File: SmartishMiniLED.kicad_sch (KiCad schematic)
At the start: 35 parts, among them J1 USB_C_Receptacle_USB2.0, J2 BUTTON, J3 Screw_Terminal_01x03, J4 Conn_01x02, P1 NeopixelStripPads, P2 NeopixelStripPads, Q1 MMBT2222, Q2 MMBT2222, Q3 IRLML6344, Q4 IRF7410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

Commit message: Added LCSC part numbers
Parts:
- C6: LCSC (none) -> C176684
- F1: LCSC (none) -> C207041
- Q1, Q2: LCSC (none) -> C2891810
- Q4: LCSC C152423 -> C148144
- R1: LCSC C17407 -> C149504
- R2, R3, R8, R9: LCSC C17617 -> C17414
- R5, R6: LCSC C139928 -> C27834
- R7: LCSC C17617 -> C352224
- U1: LCSC (none) -> C473012
- U4: LCSC C17724 -> C23654
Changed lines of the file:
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@@
       (effects (font (size 1.27 1.27)) hide)
     )
-    (property "LCSC" "C17407" (id 4) (at 67.31 40.64 0)
+    (property "LCSC" "C149504" (id 4) (at 67.31 40.64 0)
       (effects (font (size 1.27 1.27)) hide)
     )
@@
       (effects (font (size 1.27 1.27)) hide)
     )
-    (property "LCSC" "C17617" (id 4) (at 106.68 154.94 0)
+    (property "LCSC" "C17414" (id 4) (at 106.68 154.94 0)
       (effects (font (size 1.27 1.27)) hide)
     )
@@
       (effects (font (size 1.27 1.27)) hide)
     )
-    (property "LCSC" "C17617" (id 4) (at 106.68 176.53 0)
+    (property "LCSC" "C17414" (id 4) (at 106.68 176.53 0)
       (effects (font (size 1.27 1.27)) hide)
     )
@@
       (effects (font (size 1.27 1.27)) hide)
     )
-    (property "LCSC" "C139928" (id 4) (at 210.82 129.54 0)
+    (property "LCSC" "C27834" (id 4) (at 210.82 129.54 0)
       (effects (font (size 1.27 1.27)) hide)
     )
@@
       (effects (font (size 1.27 1.27)) hide)
     )
-    (property "LCSC" "C139928" (id 4) (at 219.71 129.54 0)
+    (property "LCSC" "C27834" (id 4) (at 219.71 129.54 0)
       (effects (font (size 1.27 1.27)) hide)
     )
@@
       (effects (font (size 1.27 1.27)) (justify left) hide)
     )
+    (property "LCSC" "C2891810" (id 4) (at 125.73 154.94 0)
+      (effects (font (size 1.27 1.27)) hide)
+    )
     (pin "1")
     (pin "2")
@@
     (property "Datasheet" "https://www.onsemi.com/pub/Collateral/2N3903-D.PDF" (id 3) (at 125.73 176.53 0)
       (effects (font (size 1.27 1.27)) (justify left) hide)
+    )
+    (property "LCSC" "C2891810" (id 4) (at 125.73 176.53 0)
+      (effects (font (size 1.27 1.27)) hide)
     )
     (pin "1")
@@
       (effects (font (size 1.27 1.27)) hide)
     )
-    (property "LCSC" "C17617" (id 4) (at 104.775 119.38 90)
+    (property "LCSC" "C352224" (id 4) (at 104.775 119.38 90)
       (effects (font (size 1.6002 1.6002)) hide)
     )
@@
     )
     (property "Datasheet" "https://www.espressif.com/sites/default/files/documentation/esp32-wroom-32d_esp32-wroom-32u_datasheet_en.pdf" (id 3) (at 43.18 107.95 0)
+      (effects (font (size 1.27 1.27)) hide)
+    )
+    (property "LCSC" "C473012" (id 4) (at 50.8 109.22 0)
       (effects (font (size 1.27 1.27)) hide)
     )
@@
       (effects (font (size 1.27 1.27)) hide)
     )
+    (property "LCSC" "C207041" (id 4) (at 207.01 115.57 0)
+      (effects (font (size 1.27 1.27)) hide)
+    )
     (pin "1")
     (pin "2")
@@
       (effects (font (size 1.27 1.27)) hide)
     )
-    (property "LCSC" "C17617" (id 4) (at 124.46 102.87 0)
+    (property "LCSC" "C17414" (id 4) (at 124.46 102.87 0)
       (effects (font (size 1.6002 1.6002)) hide)
     )
@@
       (effects (font (size 1.27 1.27)) hide)
     )
-    (property "LCSC" "C17617" (id 4) (at 112.395 125.73 0)
+    (property "LCSC" "C17414" (id 4) (at 112.395 125.73 0)
       (effects (font (size 1.6002 1.6002)) hide)
     )
@@
     )
     (property "Datasheet" "~" (id 3) (at 264.16 80.01 0)
+      (effects (font (size 1.27 1.27)) hide)
+    )
+    (property "LCSC" "C176684" (id 4) (at 264.16 80.01 0)
       (effects (font (size 1.27 1.27)) hide)
     )
@@
       (effects (font (size 1.27 1.27)) (justify left) hide)
     )
-    (property "LCSC" "C152423" (id 4) (at 139.065 110.49 0)
+    (property "LCSC" "C148144" (id 4) (at 139.065 110.49 0)
       (effects (font (size 1.6002 1.6002)) hide)
     )
@@
       (effects (font (size 1.27 1.27)) hide)
     )
-    (property "LCSC" "C17724" (id 4) (at 129.54 76.2 0)
+    (property "LCSC" "C23654" (id 4) (at 129.54 76.2 0)
       (effects (font (size 1.6002 1.6002)) hide)
     )

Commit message: Part position corrections
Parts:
- C6, Q1, Q2, Q3, U2, U4: JLCPCB_CORRECTION (none) -> 0;0;180
- J1: JLCPCB_CORRECTION 1.8;-0.3;180 -> (none)
- Q4, U1: JLCPCB_CORRECTION (none) -> 0;0;90
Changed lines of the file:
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@@
+      (effects (font (size 1.27 1.27)) hide)
+    )
+    (property "JLCPCB_CORRECTION" "0;0;180" (id 5) (at 80.01 36.83 0)
       (effects (font (size 1.27 1.27)) hide)
     )
@@
       (effects (font (size 1.27 1.27)) hide)
     )
-    (property "JLCPCB_CORRECTION" "1.8;-0.3;180" (id 5) (at 182.88 130.81 0)
+    (property "JLCPCB_CORRECTION" "" (id 5) (at 182.88 130.81 0)
       (effects (font (size 1.27 1.27)) hide)
     )
@@
       (effects (font (size 1.27 1.27)) hide)
     )
+    (property "JLCPCB_CORRECTION" "0;0;180" (id 5) (at 125.73 154.94 0)
+      (effects (font (size 1.27 1.27)) hide)
+    )
     (pin "1")
     (pin "2")
@@
     )
     (property "LCSC" "C2891810" (id 4) (at 125.73 176.53 0)
+      (effects (font (size 1.27 1.27)) hide)
+    )
+    (property "JLCPCB_CORRECTION" "0;0;180" (id 5) (at 125.73 176.53 0)
       (effects (font (size 1.27 1.27)) hide)
     )
@@
     (property "LCSC" "C693370" (id 4) (at 121.92 119.38 0)
       (effects (font (size 1.6002 1.6002)) hide)
+    )
+    (property "JLCPCB_CORRECTION" "0;0;180" (id 5) (at 121.92 119.38 0)
+      (effects (font (size 1.27 1.27)) hide)
     )
     (pin "1")
@@
     )
     (property "LCSC" "C473012" (id 4) (at 50.8 109.22 0)
+      (effects (font (size 1.27 1.27)) hide)
+    )
+    (property "JLCPCB_CORRECTION" "0;0;90" (id 5) (at 50.8 109.22 0)
       (effects (font (size 1.27 1.27)) hide)
     )
@@
       (effects (font (size 1.27 1.27)) hide)
     )
+    (property "JLCPCB_CORRECTION" "0;0;180" (id 5) (at 264.16 80.01 0)
+      (effects (font (size 1.27 1.27)) hide)
+    )
     (pin "1")
     (pin "2")
@@
     (property "LCSC" "C148144" (id 4) (at 139.065 110.49 0)
       (effects (font (size 1.6002 1.6002)) hide)
+    )
+    (property "JLCPCB_CORRECTION" "0;0;90" (id 5) (at 139.065 110.49 0)
+      (effects (font (size 1.27 1.27)) hide)
     )
     (pin "1")
@@
       (effects (font (size 1.6002 1.6002)) hide)
     )
-    (pin "1")
+    (property "JLCPCB_CORRECTION" "0;0;180" (id 5) (at 129.54 76.2 0)
+      (effects (font (size 1.27 1.27)) hide)
+    )
+    (pin "1")

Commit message: More position updates
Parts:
- J1: JLCPCB_CORRECTION (none) -> 0;-15;0
- Q4: JLCPCB_CORRECTION 0;0;90 -> 0;0;270
- U1: JLCPCB_CORRECTION 0;0;90 -> -10;0;270
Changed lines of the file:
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@@
       (effects (font (size 1.27 1.27)) hide)
     )
-    (property "JLCPCB_CORRECTION" "" (id 5) (at 182.88 130.81 0)
+    (property "JLCPCB_CORRECTION" "0;-15;0" (id 5) (at 182.88 130.81 0)
       (effects (font (size 1.27 1.27)) hide)
     )
@@
       (effects (font (size 1.27 1.27)) hide)
     )
-    (property "JLCPCB_CORRECTION" "0;0;90" (id 5) (at 50.8 109.22 0)
+    (property "JLCPCB_CORRECTION" "-10;0;270" (id 5) (at 50.8 109.22 0)
       (effects (font (size 1.27 1.27)) hide)
     )
@@
       (effects (font (size 1.6002 1.6002)) hide)
     )
-    (property "JLCPCB_CORRECTION" "0;0;90" (id 5) (at 139.065 110.49 0)
-      (effects (font (size 1.27 1.27)) hide)
-    )
+    (property "JLCPCB_CORRECTION" "0;0;270" (id 5) (at 139.065 110.49 0)
+      (effects (font (size 1.27 1.27)) hide)
+    )

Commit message: Updated position corrections
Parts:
- J1: JLCPCB_CORRECTION 0;-15;0 -> -5;0;0
- U1: JLCPCB_CORRECTION -10;0;270 -> 0;-5;270
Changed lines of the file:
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@@
       (effects (font (size 1.27 1.27)) hide)
     )
-    (property "JLCPCB_CORRECTION" "0;-15;0" (id 5) (at 182.88 130.81 0)
+    (property "JLCPCB_CORRECTION" "-5;0;0" (id 5) (at 182.88 130.81 0)
       (effects (font (size 1.27 1.27)) hide)
     )
@@
       (effects (font (size 1.27 1.27)) hide)
     )
-    (property "JLCPCB_CORRECTION" "-10;0;270" (id 5) (at 50.8 109.22 0)
-      (effects (font (size 1.27 1.27)) hide)
-    )
+    (property "JLCPCB_CORRECTION" "0;-5;270" (id 5) (at 50.8 109.22 0)
+      (effects (font (size 1.27 1.27)) hide)
+    )

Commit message: Updated teh version number
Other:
- title: SmartishNight -> SmartishMiniLED
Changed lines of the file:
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@@
   (paper "A4")
   (title_block
-    (title "SmartishNight")
+    (title "SmartishMiniLED")
     (date "2020-11-03")
-    (rev "1.2")
+    (rev "${version_name}")
   )
   (junction (at 124.46 110.49) (diameter 0) (color 0 0 0 0)

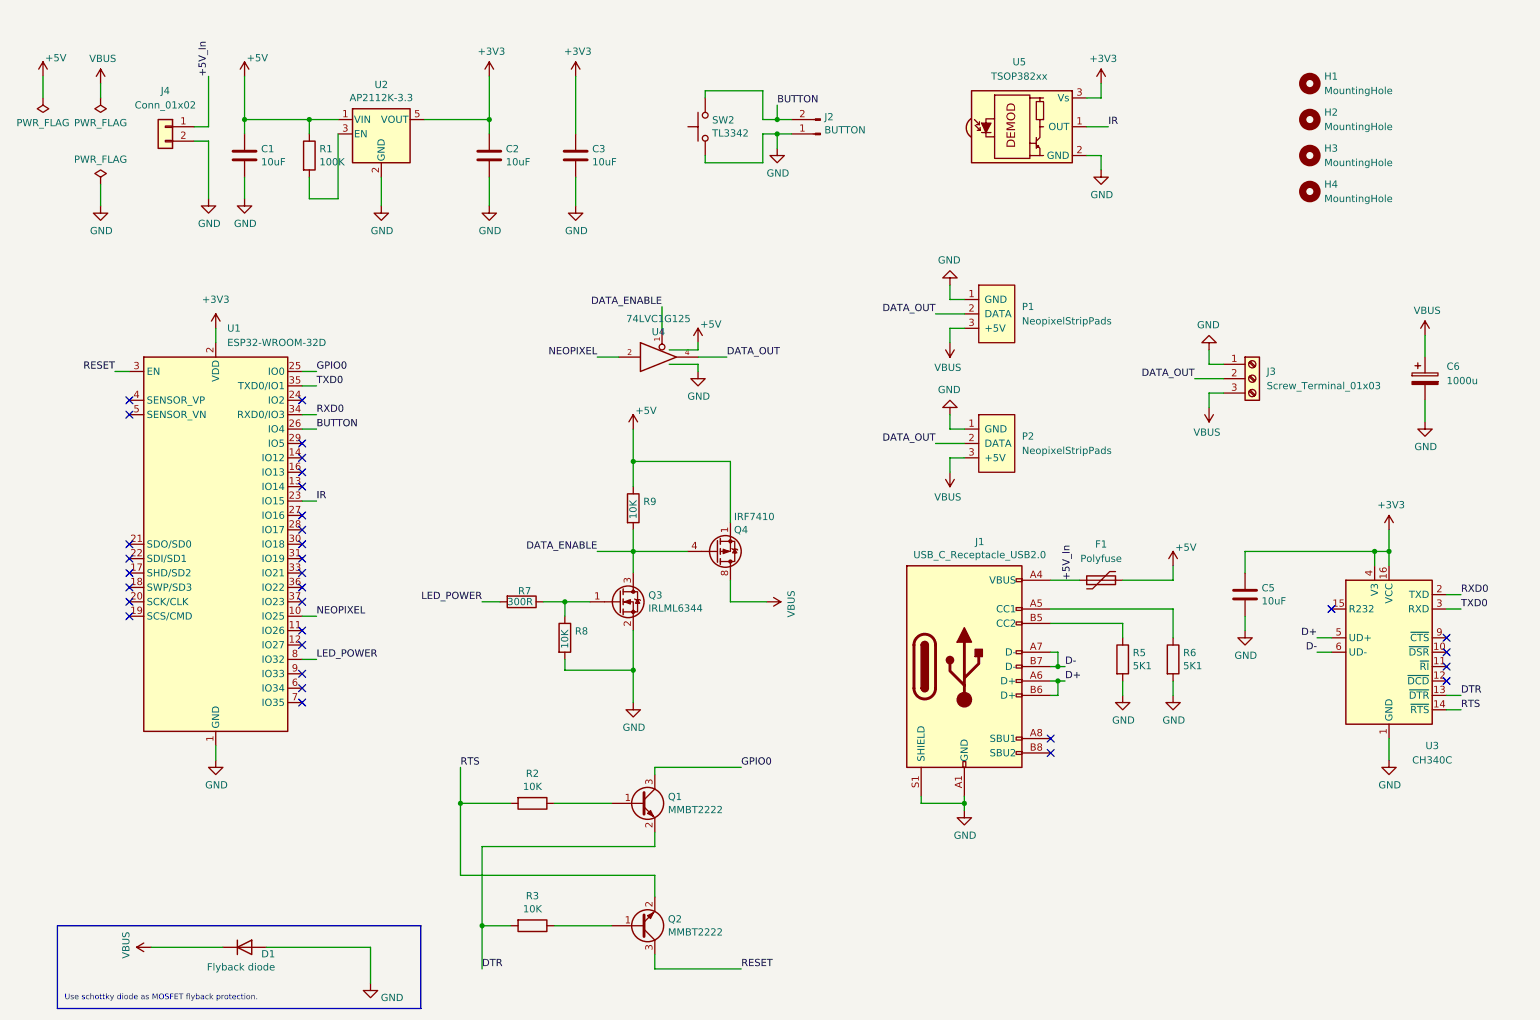
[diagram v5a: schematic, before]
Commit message: Various fixes
- Moved the capacitor to the other side of the MOSFET to fix brownout issues, fixes #4
- Added extra components needed to fix restart when programming via USB, fixes #2
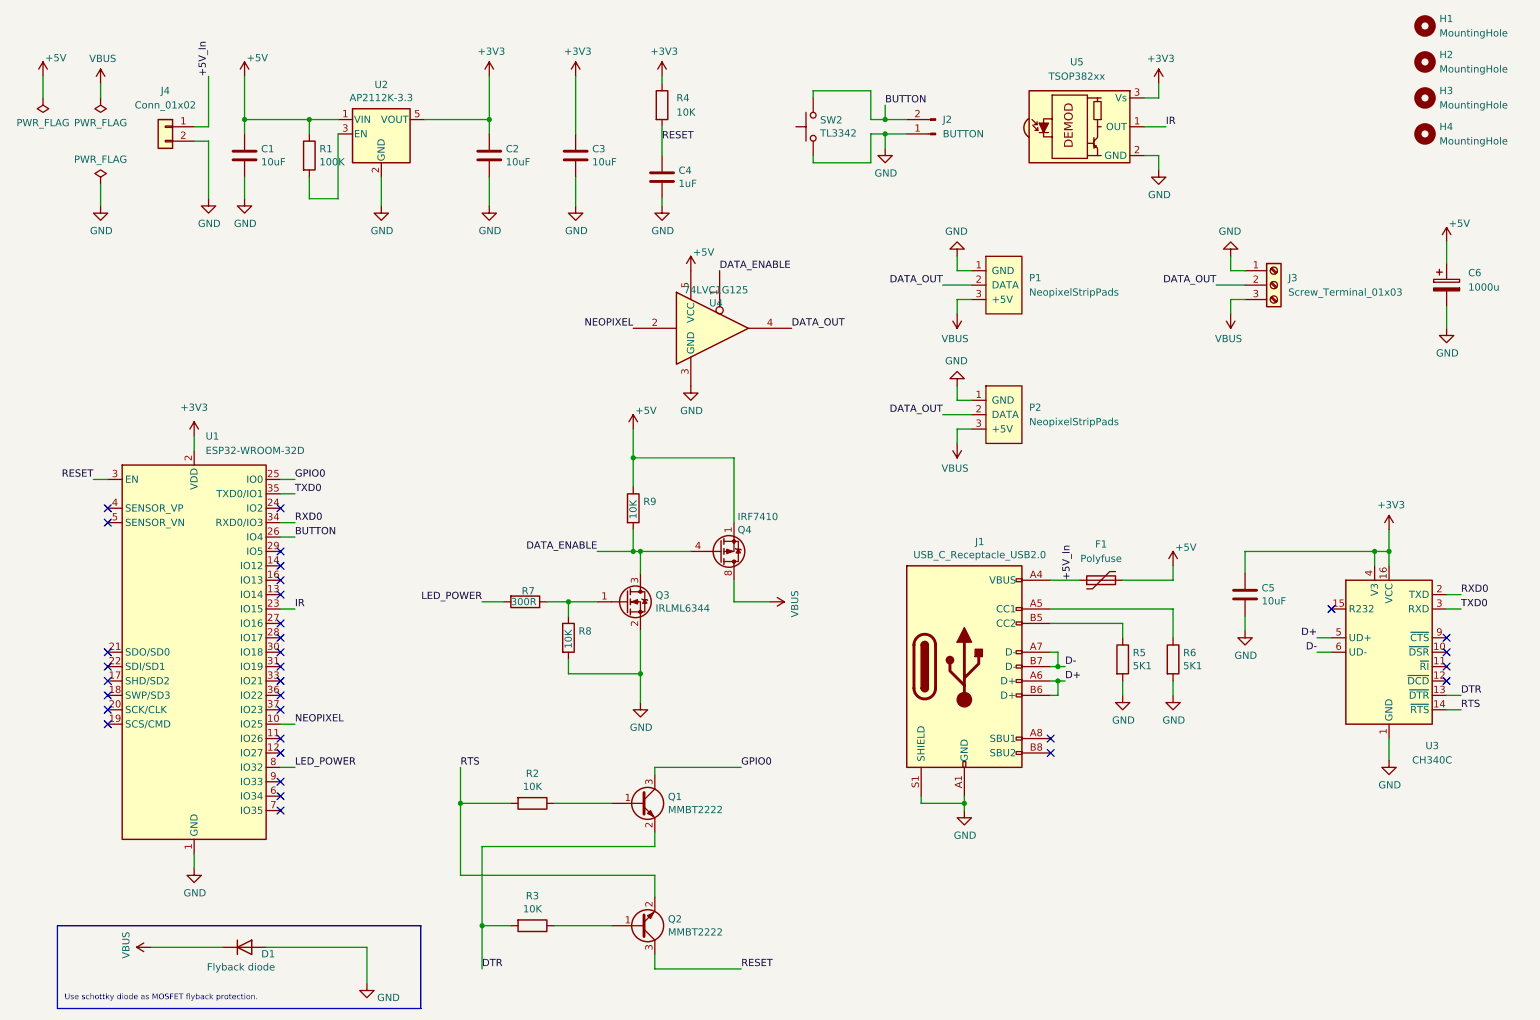
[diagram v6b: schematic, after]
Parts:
- added C4: 1uF, Capacitor_SMD:C_0805_2012Metric, symbol Device:C
- added R4: 10K, Resistor_SMD:R_0805_2012Metric, symbol Device:R
- J2: symbol Connector:Conn_01x02_Male -> Connector:Conn_01x02_Pin
- U1: footprint RF_Module:ESP32-WROOM-32 -> RF_Module:ESP32-WROOM-32D
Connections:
- net +3V3: now also R4.1
- net +5V: now also C6.1
- net GND: now also C4.2
- net RESET: now also C4.1, R4.2
- net VBUS: no longer C6.1
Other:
- moved on the sheet: C6, H1, H2, H3, H4, J2, J3, P1, P2, Q3, Q4, R7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
